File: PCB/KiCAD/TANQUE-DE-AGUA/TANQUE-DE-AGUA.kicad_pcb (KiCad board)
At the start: 2 copper layers, 81.3 x 99.1 mm, 39 parts, among them J2 Vca_OUT, J3 DC IN, J5 HX30002-BA, Q1 2N3904, SW1 Nivel MAX, SW2 Nivel Min, U1 74HC00, U2 ULN2003, U3 LM7805, U4 74HC14, U5 MOC3021M, U6 BTA16-600C

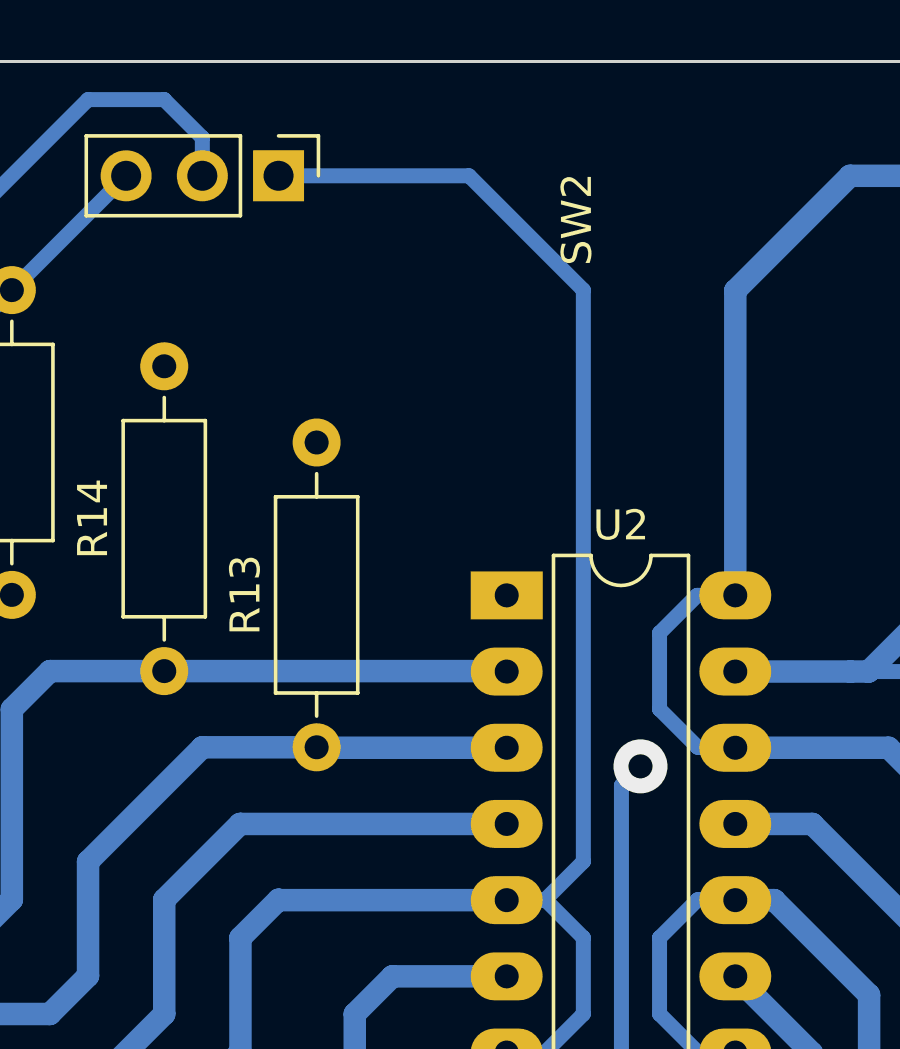
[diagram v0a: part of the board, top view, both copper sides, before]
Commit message: actualizacion del esquematico en Proteus y en KiCAD
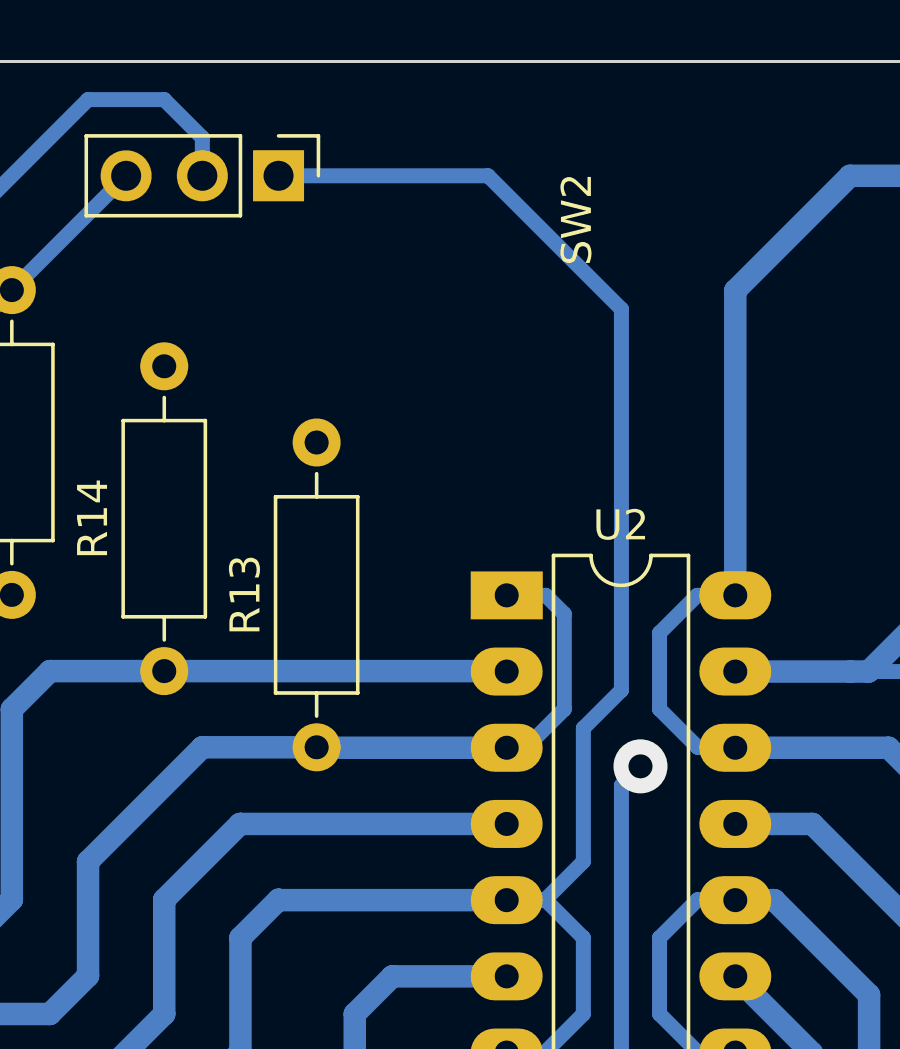
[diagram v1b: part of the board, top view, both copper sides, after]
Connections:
- net /N1 renamed /nA
- net /N3 renamed /nC
- net 11 renamed A
- net 22 renamed B
- net N22 renamed nB
- net N44 renamed nD
- net N5 renamed nE
- net Net-(J5-Pad3) renamed /E
- net Net-(J5-Pad5) renamed /D
- net Net-(J5-Pad6) renamed /C
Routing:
- net /D: track 26.0 -> 33.8 mm
- net B: track 83.3 -> 84.7 mm

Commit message: actualizacion del PCB
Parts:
- added G***: LOGO, Bitmaps:Tanque, F.Cu at (267.5, 91.6)
- added G***: LOGO, Bitmaps:Logo, F.Cu at (213.4, 110.7)
- added H1: MountingHole, MountingHole:MountingHole_2.7mm_M2.5, F.Cu at (208.3, 55.9)
- added H2: MountingHole, MountingHole:MountingHole_2.7mm_M2.5, F.Cu at (279.4, 55.9)
- added H3: MountingHole, MountingHole:MountingHole_2.7mm_M2.5, F.Cu at (279.4, 144.8)
- added H4: MountingHole, MountingHole:MountingHole_2.7mm_M2.5, F.Cu at (208.3, 144.8)
- C1, C3: footprint Capacitor_THT:CP_Radial_D6.3mm_P2.50mm -> Capacitor_THT:CP_Radial_D8.0mm_P3.50mm
- Q1: footprint Package_TO_SOT_THT:TO-92_Inline -> Package_TO_SOT_THT:TO-92_Wide
- moved BTN1 60.7 mm to (276.0, 117.6)
- moved J3 15.8 mm to (213.3, 124.5)
- moved D2 5.53 mm to (276.2, 97.8)
- moved D3 5.53 mm to (276.2, 90.2)
- moved D4 5.53 mm to (276.2, 82.5)
- moved D5 5.53 mm to (276.2, 74.9)
- moved D6 5.53 mm to (276.2, 67.3)
- moved R2 5.08 mm to (250.2, 109.2)
- moved SW1 4.58 mm to (250.2, 57.1)
- moved R12 3.94 mm to (217.2, 85.3)
- moved R11 3.89 mm to (213.4, 86.9)
- moved U3 3.00 mm to (231.4, 144.8), turned to 90 degrees
- moved Q1 2.79 mm to (255.4, 126.9), turned to 90 degrees
- moved D1 2.75 mm to (217.4, 131.8), turned to 90 degrees
- moved R14 2.75 mm to (219.5, 73.4)
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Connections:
- U1 pad 1: Net-(SW1-Pad2) -> nE
- U1 pad 2: nE -> Net-(SW1-Pad2)
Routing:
- net +5V: track 231.5 -> 323.1 mm, vias 2 -> 0
- net nE: track 78.5 -> 61.8 mm
- net Net-(U1-Pad3): track 19.9 -> 34.0 mm
- net Net-(BTN1-Pad2): track 6.91 -> 17.3 mm, vias 2 -> 0
- net Net-(Q1-Pad2): track 5.08 -> 15.4 mm
- net +12V: track 21.8 -> 29.8 mm
- net Net-(U1-Pad6): track 18.4 -> 25.7 mm
- net nD: track 36.2 -> 30.4 mm
- net Net-(D6-Pad1): track 14.1 -> 19.7 mm
- net Net-(D5-Pad1): track 14.1 -> 19.7 mm
- net Net-(D4-Pad1): track 14.1 -> 19.7 mm
- net Net-(D3-Pad1): track 14.1 -> 19.7 mm
- net Net-(D2-Pad1): track 14.1 -> 19.7 mm
- net /C: track 35.3 -> 30.2 mm
- net Net-(U1-Pad9): track 17.6 -> 13.8 mm
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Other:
- outline, holes or cut-outs redrawn
- board text added: "0 %"
- board text added: "100%"
- board text added: "20%"
- board text added: "80%"
- board text added: "Control de Carga para Tanque de Agua"
- board text added: "Nivel MAX"
- board text added: "Nivel MIN"

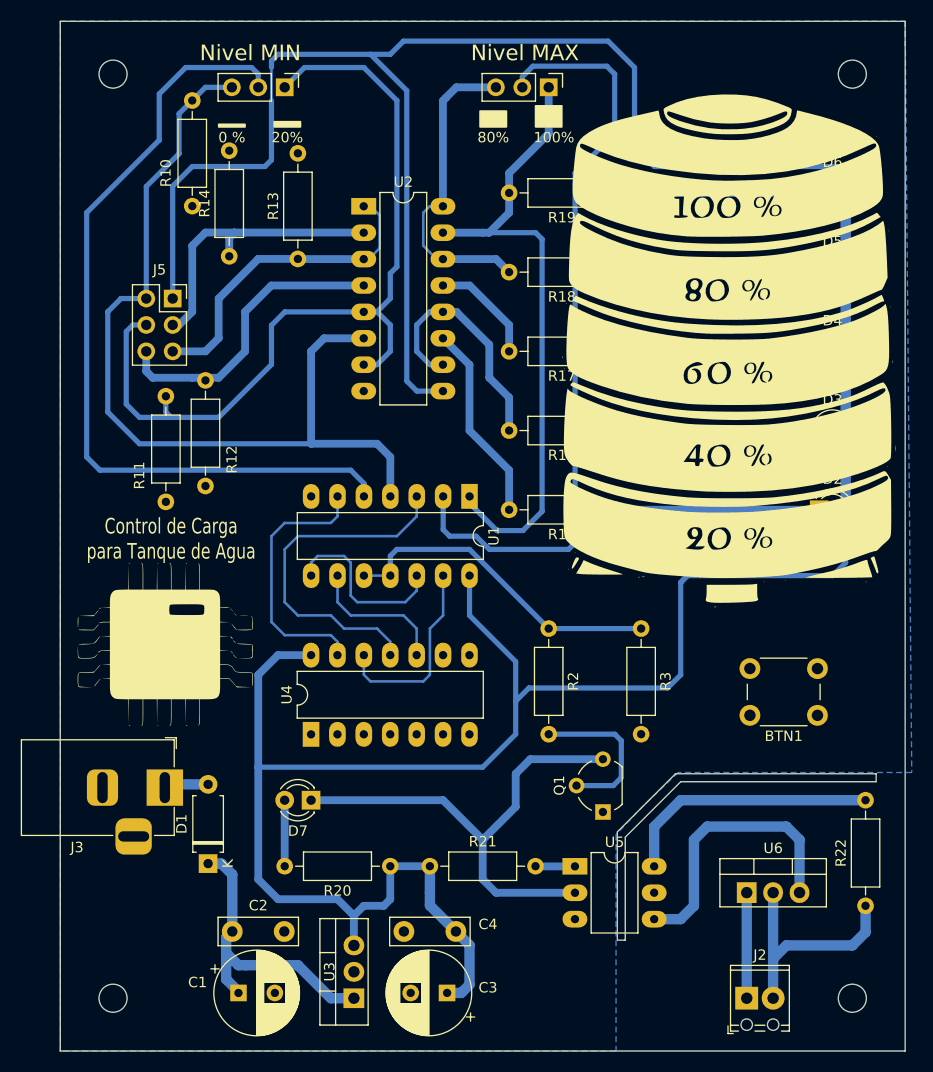
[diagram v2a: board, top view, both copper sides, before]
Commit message: se agrega Fuente capacitiva
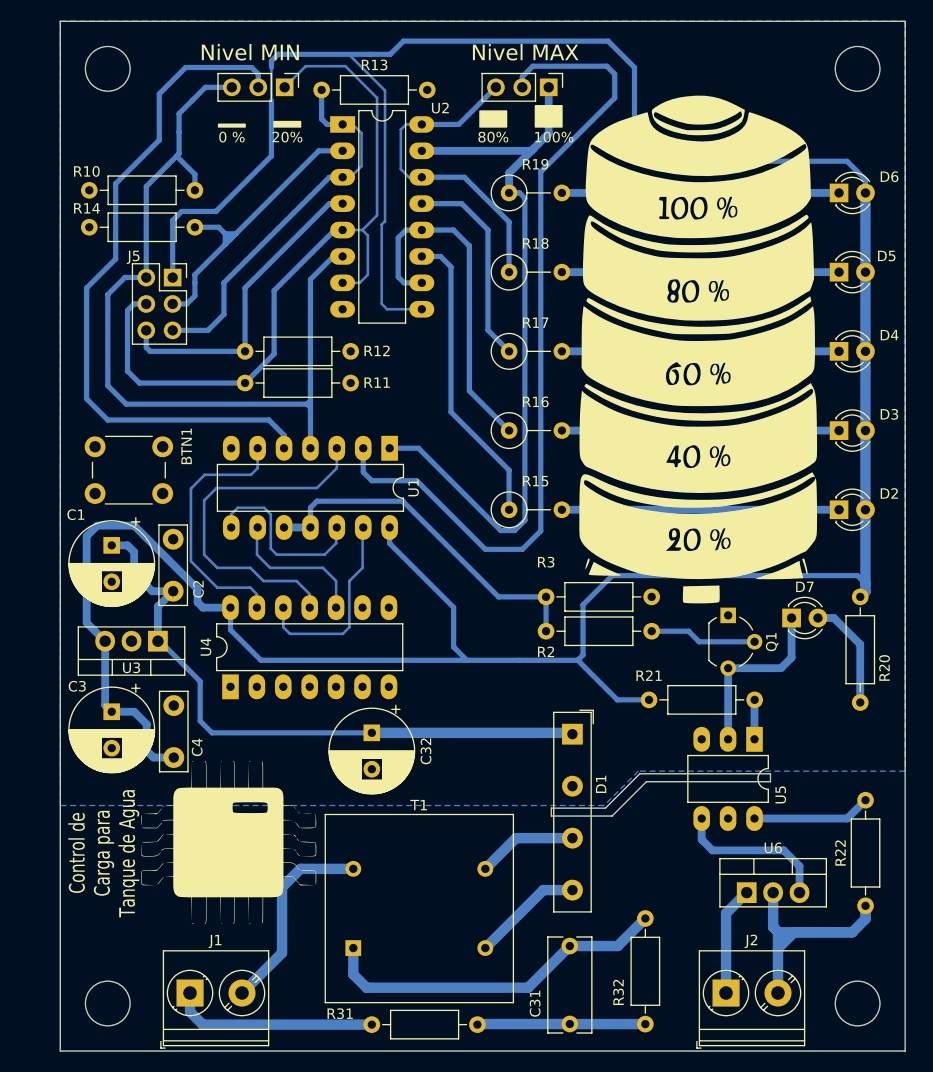
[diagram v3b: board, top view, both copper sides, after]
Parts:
- removed J3: DC IN, Connector_BarrelJack:BarrelJack_Horizontal
- added C31: 1000nF, Capacitor_THT:C_Rect_L9.0mm_W4.0mm_P7.50mm_MKT, F.Cu at (252.2, 147.3)
- added C32: 100uF, Capacitor_THT:CP_Radial_D8.0mm_P3.50mm, F.Cu at (233.2, 119.3)
- added J1: Vca_IN, TerminalBlock_Phoenix:TerminalBlock_Phoenix_PT-1,5-2-5.0-H_1x02_P5.00mm_Horizontal, F.Cu at (215.7, 144.3)
- added R31: 50R, Resistor_THT:R_Axial_DIN0207_L6.3mm_D2.5mm_P10.16mm_Horizontal, F.Cu at (233.2, 147.3)
- added R32: 1M, Resistor_THT:R_Axial_DIN0207_L6.3mm_D2.5mm_P10.16mm_Horizontal, F.Cu at (259.5, 147.3)
- added T1: Transformer_1P_1S, Transformer_THT:Transformer_NF_ETAL_1-1_P1200, F.Cu at (231.4, 140.0)
- D1: value 1N4148 -> D_Bridge_+-AA; footprint Diode_THT:D_A-405_P7.62mm_Horizontal -> Diode_THT:Diode_Bridge_19.0x3.5x10.0mm_P5.0mm
- H1, H2, H3, H4: footprint MountingHole:MountingHole_2.7mm_M2.5 -> MountingHole:MountingHole_4.3mm_M4
- J2: footprint TerminalBlock_Phoenix:TerminalBlock_Phoenix_MPT-0,5-2-2.54_1x02_P2.54mm_Horizontal -> TerminalBlock_Phoenix:TerminalBlock_Phoenix_PT-1,5-2-5.0-H_1x02_P5.00mm_Horizontal
- R15, R16, R17, R18, R19: footprint Resistor_THT:R_Axial_DIN0207_L6.3mm_D2.5mm_P10.16mm_Horizontal -> Resistor_THT:R_Axial_DIN0309_L9.0mm_D3.2mm_P5.08mm_Vertical
- moved BTN1 74.1 mm to (206.6, 91.7), turned to 0 degrees
- moved R20 52.1 mm to (280.2, 106.2), turned to -90 degrees
- moved D7 49.4 mm to (273.6, 108.2), turned to 0 degrees
- moved C1 44.7 mm to (208.2, 101.2), turned to -90 degrees
- moved C3 42.1 mm to (208.2, 117.2), turned to -90 degrees
- moved U3 39.2 mm to (212.6, 110.4), turned to 180 degrees
- moved D1 37.2 mm to (252.5, 119.4), turned to -90 degrees
- moved C2 33.2 mm to (214.1, 105.6), turned to 90 degrees
- moved C4 31.9 mm to (214.1, 121.6), turned to 90 degrees
- moved R21 26.5 mm to (259.8, 116.1)
- moved Q1 22.4 mm to (267.5, 108.0), turned to -90 degrees
- moved U5 21.2 mm to (270.0, 119.9), turned to -90 degrees
- moved G*** 20.0 mm to (219.5, 129.8)
- moved R13 16.4 mm to (228.3, 57.4), turned to 0 degrees
- moved R15 10.2 mm to (246.4, 97.8), turned to 0 degrees
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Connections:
- net +12V renamed Net-(C1-Pad1)
- D1 pad 2: Net-(D1-Pad2) -> GNDD
- R15 pad 1: Net-(D2-Pad1) -> /nA
- R15 pad 2: /nA -> Net-(D2-Pad1)
- R16 pad 1: Net-(D3-Pad1) -> nB
- R16 pad 2: nB -> Net-(D3-Pad1)
- R17 pad 1: Net-(D4-Pad1) -> /nC
- R17 pad 2: /nC -> Net-(D4-Pad1)
- R18 pad 1: Net-(D5-Pad1) -> nD
- R18 pad 2: nD -> Net-(D5-Pad1)
- R19 pad 1: Net-(D6-Pad1) -> nE
- R19 pad 2: nE -> Net-(D6-Pad1)
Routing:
- net Net-(C31-Pad2): track 0.00 -> 33.9 mm
- net Net-(D7-Pad1): track 47.9 -> 17.2 mm
- net Net-(C1-Pad1): track 29.8 -> 60.3 mm
- net Net-(J1-Pad1): track 0.00 -> 19.8 mm
- net Net-(J1-Pad2): track 0.00 -> 19.4 mm
- net +5V: track 323.1 -> 305.3 mm
- net Net-(C31-Pad1): track 0.00 -> 16.2 mm
- net /E: track 43.5 -> 29.6 mm
- net Net-(R22-Pad2): track 25.2 -> 11.4 mm
- net B: track 85.2 -> 72.2 mm
- net Net-(SW2-Pad2): track 78.9 -> 66.0 mm
- net Net-(U5-Pad4): track 27.0 -> 15.0 mm
- net Net-(D1-Pad4): track 0.00 -> 10.7 mm
- net nE: track 61.8 -> 72.0 mm
- net nB: track 23.5 -> 33.4 mm
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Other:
- outline, holes or cut-outs redrawn

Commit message: update PCB
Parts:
- removed the G*** at (264.7, 91.7)
- added G1: LOGO, Bitmaps:Tanque, F.Cu at (264.4, 92.2)
- R15, R16, R17, R18, R19: footprint Resistor_THT:R_Axial_DIN0309_L9.0mm_D3.2mm_P5.08mm_Vertical -> Resistor_THT:R_Axial_DIN0204_L3.6mm_D1.6mm_P5.08mm_Horizontal
- moved R15 18.6 mm to (244.6, 79.2)
- moved R16 14.6 mm to (244.6, 75.7)
- moved R17 10.6 mm to (244.6, 72.1)
- moved R18 6.53 mm to (244.9, 68.6)
- moved R19 2.54 mm to (244.9, 65.3)
- moved D2 1.52 mm to (279.6, 97.8)
- moved D3 1.52 mm to (279.6, 90.2)
- moved D4 1.52 mm to (279.6, 82.5)
- moved D5 1.52 mm to (279.6, 74.9)
- moved D6 1.52 mm to (279.6, 67.3)
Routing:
- net /nA: track 28.9 -> 9.03 mm
- net nB: track 33.4 -> 17.5 mm
- net Net-(SW1-Pad2): track 80.7 -> 65.0 mm
- net nE: track 72.0 -> 56.9 mm
- net Net-(D2-Pad1): track 26.7 -> 39.3 mm
- net /nC: track 19.9 -> 8.19 mm
- net Net-(D3-Pad1): track 26.7 -> 37.5 mm
- net Net-(D4-Pad1): track 26.7 -> 35.8 mm
- net Net-(D5-Pad1): track 26.7 -> 33.7 mm
- net nD: track 32.0 -> 25.0 mm
- net +5V: track 305.3 -> 309.9 mm
- net Net-(D6-Pad1): track 26.7 -> 30.6 mm
